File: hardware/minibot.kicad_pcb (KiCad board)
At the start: 2 copper layers, 45 x 40 mm, 65 parts, among them J1 USB_OTG, J10 CONN_01X01, J11 CONN_01X01, J12 CONN_01X01, J13 CONN_01X01, J14 CONN_01X01, J15 CONN_01X01, J16 CONN_01X01, J17 CONN_01X01, J2 RESET, J3 CONN_01X18, J4 BAUD, J5 CONN_01X05, J6 CONN_01X02, J7 CONN_01X10, J8 CONN_01X01, J9 CONN_01X01, SW1 BOOT, SW2 RESET, U1 LSM6DS3US, U2 TLV70233DBV, U3 RN41, U4 STM32F411CEUx, Y1 12MHz

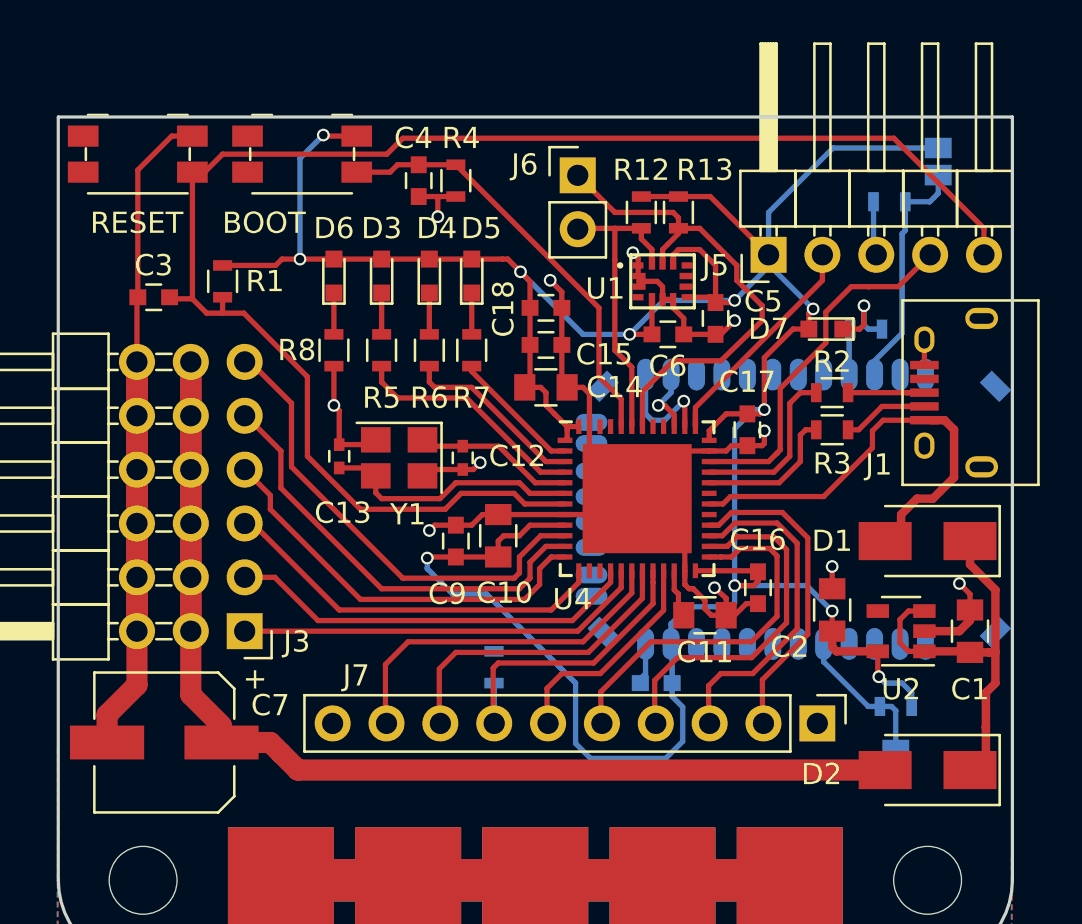
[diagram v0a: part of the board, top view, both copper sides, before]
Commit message: Fix the USB overlapping with the RN41
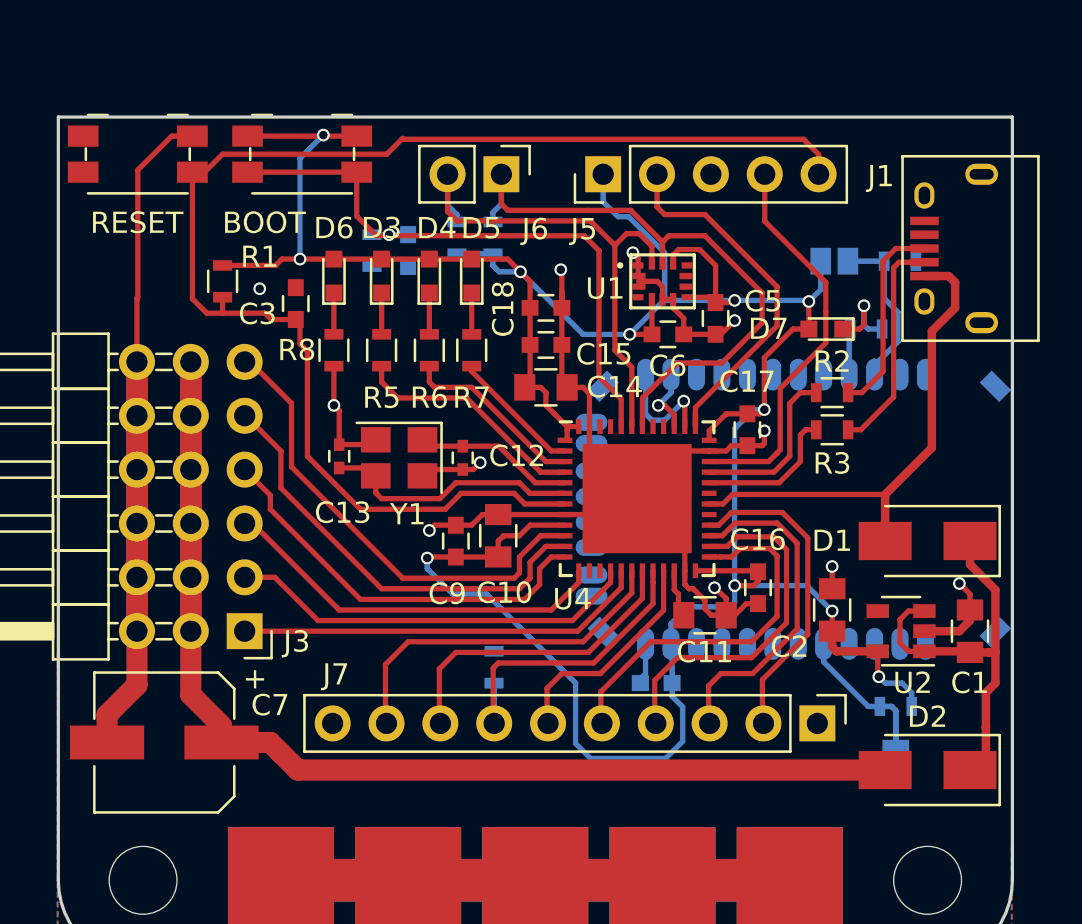
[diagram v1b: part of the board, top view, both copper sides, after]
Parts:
- C4, R12, R13, R4: moved to B.Cu
- J5: footprint Pin_Headers:Pin_Header_Angled_1x05_Pitch2.54mm -> Pin_Headers:Pin_Header_Straight_1x05_Pitch2.54mm
- moved R13 8.83 mm to (220.5, 55.7), turned to 270 degrees
- moved R12 8.78 mm to (218.8, 55.7), turned to 270 degrees
- moved J5 8.68 mm to (225.7, 52.7)
- moved J1 6.80 mm to (242.2, 56.2)
- moved J4 6.79 mm to (236.6, 56.8), turned to 90 degrees
- moved C3 6.71 mm to (211.2, 58.8), turned to 90 degrees
- moved R4 5.15 mm to (214.8, 56.3)
- moved J6 3.60 mm to (220.9, 52.7), turned to 270 degrees
- moved C4 3.34 mm to (216.5, 56.3)
- moved R11 2.84 mm to (239.7, 56.8), turned to 180 degrees
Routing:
- net /PB7: track 14.6 -> 24.6 mm
- net /BOOT: track 20.4 -> 29.8 mm, vias 0 -> 1
- net /nRST: track 73.2 -> 64.0 mm
- net /PA14: track 11.2 -> 17.6 mm
- net Net-(J1-Pad2): track 4.51 -> 10.4 mm
- net /PB6: track 23.3 -> 29.0 mm
- net Net-(J1-Pad3): track 4.05 -> 9.46 mm
- net GND: track 149.6 -> 144.2 mm, vias 11 -> 10
- net +3V3: track 150.8 -> 146.9 mm
- net /PA9: track 20.6 -> 23.6 mm
- net Net-(J4-Pad1): track 11.3 -> 8.43 mm
- net Net-(J2-Pad1): track 7.06 -> 9.76 mm
- net /PA13: track 17.1 -> 18.7 mm
- net (no net): vias 0 -> 1

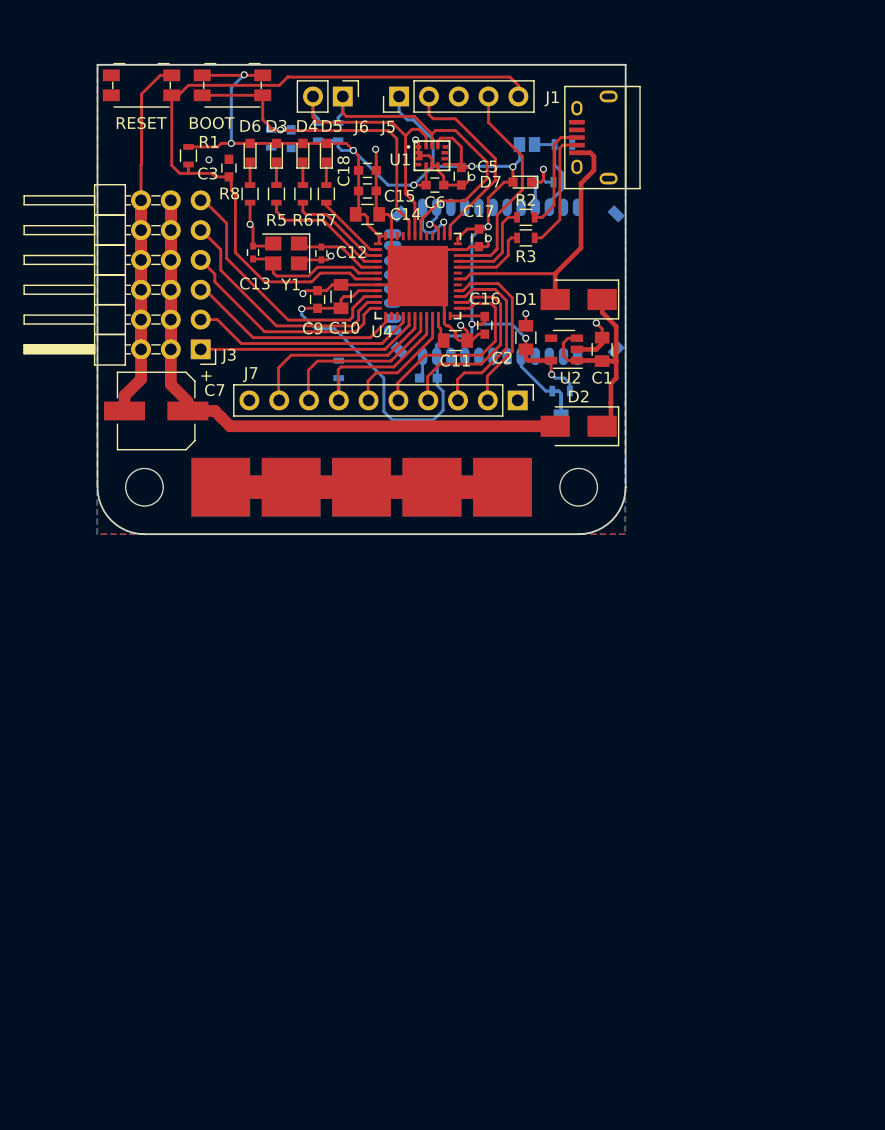
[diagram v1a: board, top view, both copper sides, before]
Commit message: Layed board out for the third time. Doesn't include power traces yet.
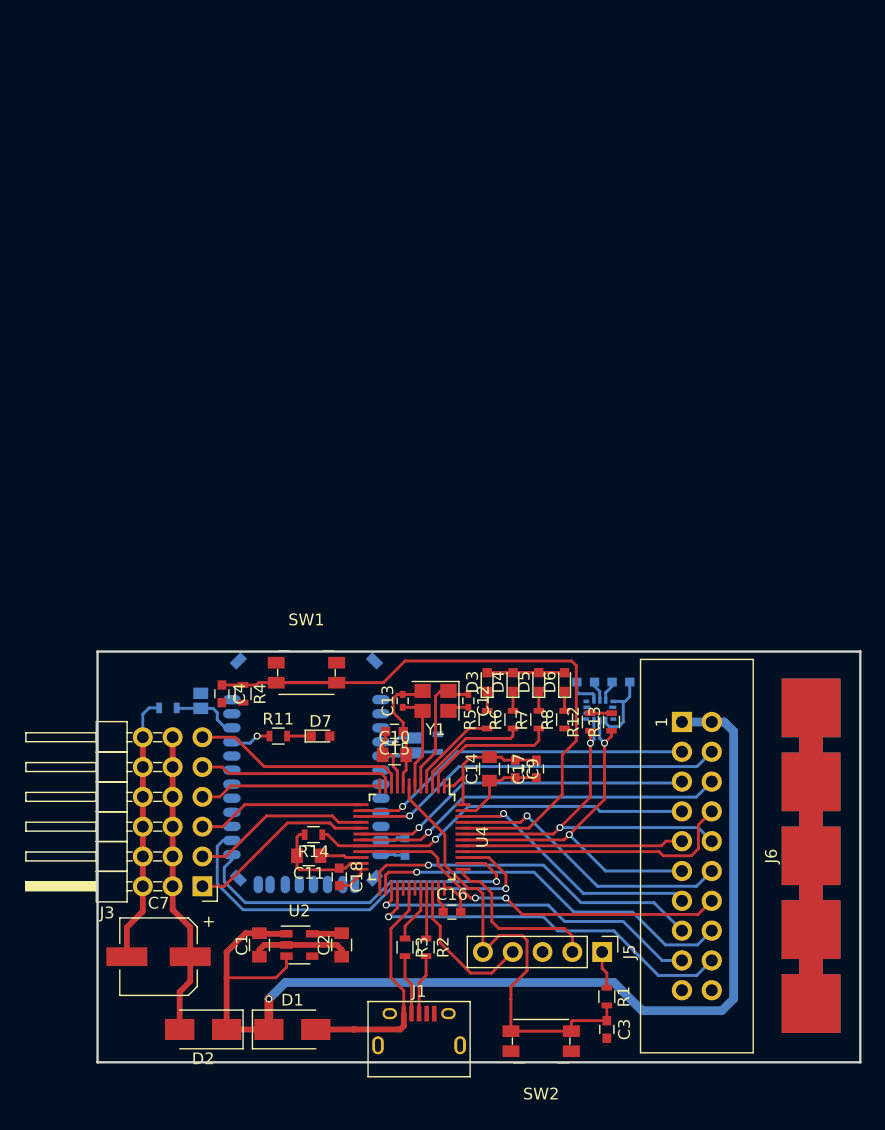
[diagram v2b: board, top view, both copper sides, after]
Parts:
- removed J7: CONN_01X10, Pin_Headers:Pin_Header_Straight_1x10_Pitch2.54mm
- removed REF** (x2): MountingHole_3.2mm_M3, Mounting_Holes:MountingHole_3.2mm_M3
- C4, R12, R13, R14, R4: moved to F.Cu
- C5, C6: moved to B.Cu
- J3: footprint modules:Pin_Header_Angled_3x06_Pitch2.54mm -> parts:Pin_Header_Angled_3x06_Pitch2.54mm
- J6: value CONN_01X02 -> Conn_01x20; footprint Pin_Headers:Pin_Header_Straight_1x02_Pitch2.54mm -> Connectors:IDC_Header_Straight_20pins
- R10: value 100 -> 10k
- R11: value 10k -> 100; moved to F.Cu
- U1: value LSM6DS3US -> RN41; footprint modules:LSM6DS3US -> parts:RN41; moved to B.Cu
- U3: value RN41 -> LSM6DS3US; footprint modules:RN41 -> parts:LSM6DS3US
- U4: footprint Housings_DFN_QFN:QFN-48-1EP_7x7mm_Pitch0.5mm -> Housings_QFP:TQFP-48_7x7mm_Pitch0.5mm
- moved J14 104.9 mm to (320.4, 123.9)
- moved J15 97.7 mm to (311.4, 109.4)
- moved J13 90.2 mm to (310.4, 123.9)
- moved J17 90.0 mm to (321.4, 109.4)
- moved J16 89.5 mm to (294.1, 117.9)
- moved SW2 88.3 mm to (237.8, 133.2), turned to 180 degrees
- moved C3 80.2 mm to (243.4, 132.2), turned to 270 degrees
- moved R1 80.0 mm to (243.4, 129.4)
- moved J1 77.4 mm to (227.4, 132.2), turned to 0 degrees
- moved J5 74.9 mm to (243.0, 125.6), turned to 270 degrees
- moved J8 68.0 mm to (270.2, 118.6), turned to 90 degrees
- moved D1 66.8 mm to (216.6, 132.2), turned to 0 degrees
- moved J10 63.6 mm to (270.4, 127.8), turned to 90 degrees
- moved R2 62.8 mm to (228.0, 125.2), turned to 270 degrees
- moved U1 62.5 mm to (224.4, 120.1), turned to 180 degrees
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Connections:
- J6 pad 1: /PB6 -> +5V
- J6 pad 2: /PB7 -> +5V
- R10 pad 1: Net-(R10-Pad1) -> GND
- R10 pad 2: Net-(D7-Pad1) -> Net-(J4-Pad1)
- R11 pad 1: GND -> Net-(R11-Pad1)
- R11 pad 2: Net-(J4-Pad1) -> Net-(D7-Pad1)
- U1 pad 10: Net-(U1-Pad10) -> (no net)
- U1 pad 11: (no net) -> +3V3
- U1 pad 12: +3V3 -> GND
- U1 pad 13: /PB6 -> /BT_TXD
- U1 pad 14: /PB7 -> /BT_RXD
- U1 pad 2: GND -> (no net)
- U1 pad 4: Net-(U1-Pad4) -> GND
- U1 pad 5: +3V3 -> Net-(J2-Pad1)
- U1 pad 6: GND -> (no net)
- U1 pad 7: GND -> (no net)
- U1 pad 8: +3V3 -> (no net)
- U1 pad 9: Net-(U1-Pad9) -> (no net)
- U3 pad 10: (no net) -> Net-(U3-Pad10)
- U3 pad 11: +3V3 -> (no net)
- U3 pad 12: GND -> +3V3
- U3 pad 13: /BT_TXD -> /PB6
- U3 pad 14: /BT_RXD -> /PB7
- U3 pad 2: (no net) -> GND
- U3 pad 4: GND -> Net-(U3-Pad4)
- U3 pad 5: Net-(J2-Pad1) -> +3V3
- U3 pad 6: (no net) -> GND
- U3 pad 7: (no net) -> GND
- U3 pad 8: (no net) -> +3V3
- U3 pad 9: (no net) -> Net-(U3-Pad9)
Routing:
- net +3V3: track 146.9 -> 55.6 mm, vias 11 -> 0
- net +5V: track 18.7 -> 94.1 mm, vias 0 -> 1
- net GND: track 144.2 -> 73.3 mm, vias 10 -> 0
- net Net-(C7-Pad1): track 62.3 -> 25.9 mm
- net /BT_RXD: track 2.78 -> 36.4 mm
- net /PA5: track 0.00 -> 32.2 mm, vias 0 -> 1
- net /PA4: track 0.00 -> 29.4 mm, vias 0 -> 1
- net /BOOT: track 29.8 -> 57.5 mm, vias 1 -> 0
- net /BT_TXD: track 5.37 -> 31.1 mm
- net /PB8: track 0.00 -> 24.4 mm, vias 0 -> 1
- net /PB4: track 0.00 -> 24.2 mm
- net /nRST: track 64.0 -> 40.4 mm
- net /PB10: track 9.94 -> 32.9 mm, vias 0 -> 2
- net /PB9: track 0.00 -> 21.9 mm, vias 0 -> 1
- net /PB5: track 0.00 -> 18.8 mm
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- removed copper zone on B.Cu, net GND
- removed copper zone on F.Cu, net GND
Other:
- board size 45 x 40 mm -> 65 x 35 mm
- board text removed: "BAUD"
- board text removed: "BOOT"
- board text removed: "RESET"

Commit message: Finish routing the board again
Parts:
- added REF**: MountingHole_3mm, Mounting_Holes:MountingHole_3mm, F.Cu at (242.0, 117.5)
- added REF**: MountingHole_3mm, Mounting_Holes:MountingHole_3mm, F.Cu at (203.0, 132.0)
- added REF**: MountingHole_3mm, Mounting_Holes:MountingHole_3mm, F.Cu at (203.0, 103.0)
- moved C7 2.21 mm to (207.3, 125.3)
- moved J4 2.14 mm to (208.4, 102.1)
- moved D1 1.80 mm to (218.4, 132.2)
- moved D2 1.70 mm to (210.7, 132.2)
- moved R10 1.70 mm to (207.7, 104.8)
- moved U2 1.41 mm to (218.6, 124.8)
- moved C1 1.41 mm to (215.2, 124.8)
- moved C2 1.41 mm to (222.2, 124.8)
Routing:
- net +3V3: track 55.6 -> 204.3 mm, vias 0 -> 9
- net GND: track 73.3 -> 104.4 mm, vias 0 -> 6
- net Net-(C7-Pad1): track 25.9 -> 40.3 mm
- net +5V: track 94.1 -> 100.3 mm
- net /PB8: track 24.4 -> 27.9 mm
- net /PB4: track 24.2 -> 27.1 mm
- net /PB9: track 21.9 -> 24.2 mm
- net /PA9: track 20.7 -> 18.6 mm
- net /PB5: track 18.8 -> 20.8 mm
- net /PB2: track 32.6 -> 33.8 mm
- net /PB1: track 31.9 -> 32.9 mm
- net /PB7: track 33.3 -> 32.6 mm
- added copper zone on B.Cu, net GND
- added copper zone on F.Cu, net GND
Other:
- outline, holes or cut-outs redrawn
- board text added: "BAUD"
- board text added: "RESET"
